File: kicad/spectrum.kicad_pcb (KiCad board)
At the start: 2 copper layers, 256 parts, among them J1 SUPPLY, J2 Input, J3 Output, SW1 POWER, SW2 RIGHT SOURCE, SW3 LEFT SOURCE, U1 LM833, U10 LM833, U11 LM833, U12 LM833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

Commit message: Organize parts
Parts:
- moved PTL13 341.7 mm to (389.4, 66.8), turned to 90 degrees
- moved R86 322.5 mm to (394.8, 169.2), turned to 180 degrees
- moved R66 298.8 mm to (386.2, 32.4)
- moved R117 296.2 mm to (371.4, 118.6)
- moved C30 287.1 mm to (389.1, 160.4)
- moved U15 286.4 mm to (356.4, 101.7)
- moved PTL14 282.7 mm to (375.6, 65.0), turned to 90 degrees
- moved R116 280.5 mm to (386.6, 118.6)
- moved PTL18 276.1 mm to (322.2, 68.8), turned to 90 degrees
- moved PTL15 270.5 mm to (361.0, 68.0), turned to 90 degrees
- moved U13 266.9 mm to (385.6, 100.4)
- moved U16 263.1 mm to (343.0, 102.4)
- moved R108 261.5 mm to (356.2, 130.2)
- moved R89 252.6 mm to (341.0, 169.8)
- moved R109 252.4 mm to (339.8, 130.0)
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
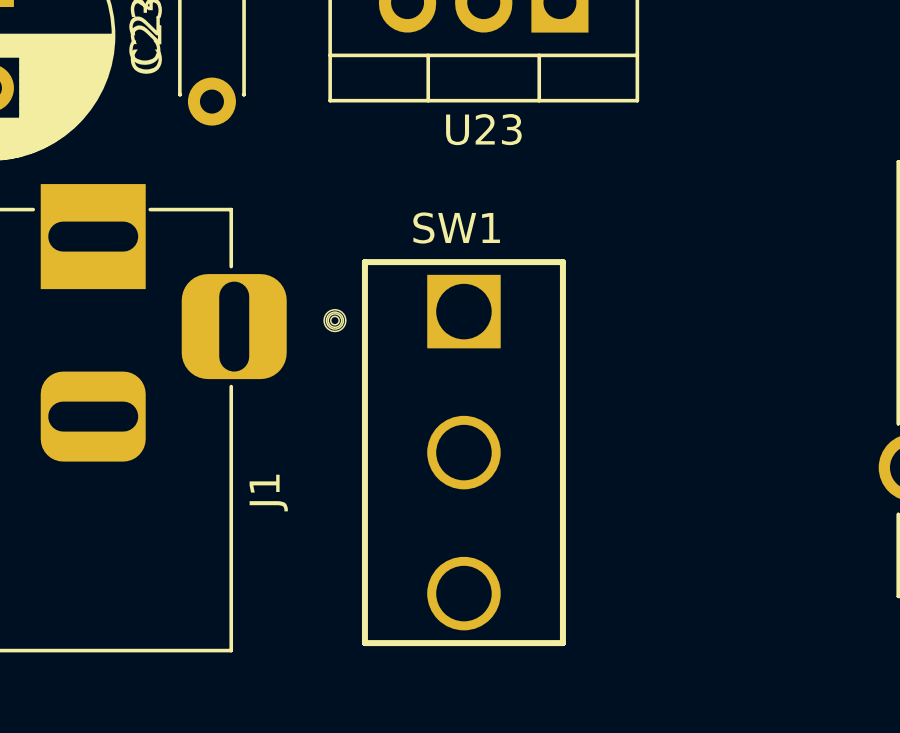
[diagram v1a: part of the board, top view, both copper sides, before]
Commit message: Fix POT footprint and pins
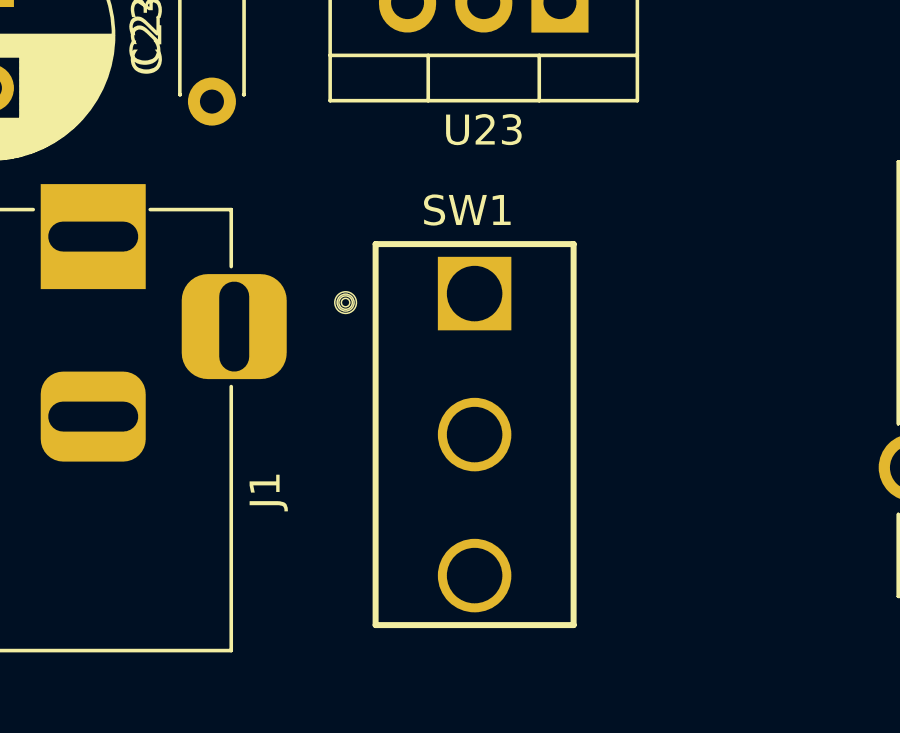
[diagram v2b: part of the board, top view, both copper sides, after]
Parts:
- moved SW1 0.70 mm to (219.0, 262.0)

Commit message: Filter array component layout
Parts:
- added TP28: Vpreamp_L, TestPoint:TestPoint_Keystone_5000-5004_Miniature, F.Cu at (164.2, 114.4)
- added TP29: Vpreamp_R, TestPoint:TestPoint_Keystone_5000-5004_Miniature, F.Cu at (272.4, 163.0)
- moved R51 182.1 mm to (187.4, 111.8), turned to 180 degrees
- moved TP12 176.5 mm to (170.4, 111.4)
- moved R50 170.3 mm to (187.0, 105.6), turned to 180 degrees
- moved TP11 164.7 mm to (170.4, 106.2)
- moved R49 160.8 mm to (188.2, 99.6), turned to 180 degrees
- moved TP10 159.2 mm to (170.2, 100.4)
- moved R48 153.8 mm to (188.8, 93.4), turned to 180 degrees
- moved TP9 153.8 mm to (170.0, 94.4)
- moved TP8 152.5 mm to (170.4, 86.8)
- moved TP3 151.2 mm to (170.4, 58.6)
- moved TP7 149.5 mm to (170.8, 80.8)
- moved TP5 148.8 mm to (170.6, 68.4)
- moved TP4 148.7 mm to (170.4, 62.8)
- moved TP6 146.6 mm to (171.0, 74.6)
- moved R46 141.6 mm to (188.4, 82.2), turned to 180 degrees
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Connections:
- C1 pad 1: Vin_L -> Vsrc_L
- C1 pad 2: Net-(C1-Pad2) -> Vin_L
- C50 pad 1: Vin_R -> Vsrc_R
- C50 pad 2: Net-(C50-Pad2) -> Vin_R
- J2 pad R: Vin_R -> Vsrc_R
- J2 pad T: Vin_L -> Vsrc_L
- R1 pad 2: Net-(C1-Pad2) -> Vin_L
- R126 pad 2: Net-(C50-Pad2) -> Vin_R
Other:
- board text added: "1 kHz"
- board text added: "125 Hz"
- board text added: "16 kHz"
- board text added: "2 kHz"
- board text added: "250 Hz"
- board text added: "31.5 Hz"
- board text added: "4 kHz"
- board text added: "500 Hz"
- board text added: "63 Hz"
- board text added: "8 kHz"
- board text added: "Preamp"

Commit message: Fix bypass routes
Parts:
- moved TP28 6.21 mm to (170.2, 116.0)
- moved R52 5.80 mm to (140.0, 55.2)
- moved R57 5.80 mm to (111.2, 55.6)
- moved R59 5.80 mm to (97.2, 54.2)
- moved R65 5.80 mm to (153.6, 55.2)
- moved R53 5.80 mm to (69.6, 54.0)
- moved R55 5.80 mm to (123.2, 55.4)
- moved R56 5.80 mm to (58.0, 53.4)
- moved R58 5.80 mm to (46.4, 53.4)
- moved R60 5.80 mm to (35.0, 53.0)
- moved R61 5.80 mm to (82.8, 54.0)
- moved R62 5.80 mm to (23.2, 52.8)
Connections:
- C1 pad 1: Vsrc_L -> Vin_L
- C1 pad 2: Vin_L -> Net-(C1-Pad2)
- C50 pad 1: Vsrc_R -> Vin_R
- C50 pad 2: Vin_R -> Net-(C50-Pad2)
- J2 pad R: Vsrc_R -> Vin_R
- J2 pad T: Vsrc_L -> Vin_L
- R1 pad 2: Vin_L -> Net-(C1-Pad2)
- R126 pad 2: Vin_R -> Net-(C50-Pad2)

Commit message: More component layout
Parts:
- moved TP17 213.9 mm to (241.3, 48.6)
- moved R76 213.9 mm to (226.9, 48.4)
- moved TP18 199.7 mm to (241.1, 54.4)
- moved R77 193.2 mm to (229.2, 54.6)
- moved TP19 185.8 mm to (240.1, 61.2)
- moved R78 180.1 mm to (228.4, 61.8)
- moved TP20 168.4 mm to (240.6, 67.7)
- moved R79 164.8 mm to (228.3, 68.2)
- moved TP21 155.4 mm to (240.6, 74.8)
- moved R80 152.3 mm to (226.6, 75.1)
- moved TP22 143.1 mm to (239.2, 80.9)
- moved R81 141.9 mm to (224.2, 82.0)
- moved TP23 133.6 mm to (238.1, 87.1)
- moved R82 130.3 mm to (224.1, 87.2)
- moved TP24 121.1 mm to (237.7, 93.2)
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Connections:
- U1 pad 1: Net-(PTL1-Pad2) -> Net-(C22-Pad1)
- U1 pad 2: Net-(PTL1-Pad1) -> Net-(R42-Pad1)
- U1 pad 6: Net-(R42-Pad1) -> Net-(PTL1-Pad1)
- U1 pad 7: Net-(C22-Pad1) -> Net-(PTL1-Pad2)

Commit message: Finish component layout and add extra 7805
- Extra 7805 needed for heat dissipation
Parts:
- added C51: 0.1uF, Capacitor_THT:C_Disc_D4.3mm_W1.9mm_P5.00mm, F.Cu at (183.4, 182.1)
- added C52: 0.1uF, Capacitor_THT:C_Disc_D4.3mm_W1.9mm_P5.00mm, F.Cu at (230.0, 182.9)
- added T1: SP-70, Triad_Magnetics_SP-70:SP70, F.Cu at (218.0, 173.3)
- added T2: SP-70, Triad_Magnetics_SP-70:SP70, F.Cu at (194.6, 178.1)
- added U24: L7805, Package_TO_SOT_THT:TO-220-3_Vertical, F.Cu at (214.9, 160.0)
- R1, R126: value 1K -> 6.2K
- R54, R73: value 10K -> 51K
- moved R66 87.9 mm to (369.5, 127.3)
- moved R71 86.9 mm to (280.7, 127.2)
- moved R68 86.7 mm to (357.0, 127.3)
- moved R75 86.0 mm to (319.2, 127.3)
- moved R72 85.7 mm to (331.9, 127.3)
- moved R70 85.7 mm to (344.4, 127.3)
- moved R67 85.7 mm to (306.5, 127.2)
- moved R69 85.2 mm to (293.4, 127.2)
- moved R74 84.1 mm to (267.7, 127.2)
- moved R127 83.1 mm to (254.9, 127.3)
- moved R76 82.6 mm to (219.2, 130.6)
- moved TP17 82.5 mm to (231.7, 130.6)
- moved TP18 80.8 mm to (231.7, 134.6)
- moved R77 80.6 mm to (219.2, 134.6)
- moved PTL14 79.6 mm to (360.8, 151.8)
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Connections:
- J2 pad R: Vin_R -> Net-(J2-PadR)
- J2 pad S: GNDREF -> Net-(J2-PadS)
- J2 pad T: Vin_L -> Net-(J2-PadT)
- U12 pad 1: Net-(PTL12-Pad2) -> Net-(C29-Pad1)
- U12 pad 2: Net-(PTL12-Pad1) -> Net-(R73-Pad2)
- U12 pad 6: Net-(R73-Pad2) -> Net-(PTL12-Pad1)
- U12 pad 7: Net-(C29-Pad1) -> Net-(PTL12-Pad2)
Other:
- board text added: "5V"
- board text added: "GND"
- board text added: "LEFT INPUT"
- board text added: "LEFT OUTPUT"
- board text added: "RIGHT INPUT"
- board text added: "RIGHT OUTPUT"
- board text added: "VGND"
